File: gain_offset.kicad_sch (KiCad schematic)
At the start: 30 parts, among them U3 AD8337BCPZ-REEL-ND, U4 LMH6551MA, U5 AD8337BCPZ-REEL-ND, U7 LMH6551MA

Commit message: Save work on simplifying the desing
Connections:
- net CH2_COMMON is gone; now on net +1V5: C14.1, U4.2 (VCM)
- net CH1_COMMON renamed +1V5
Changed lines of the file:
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@@
 		)
 	)
-	(global_label "CH2_COMMON"
-		(shape input)
-		(at 168.91 113.03 180)
+	(global_label "AN_TRIGGER_CH1"
+		(shape output)
+		(at 138.43 38.1 0)
 		(fields_autoplaced yes)
 		(effects
@@
 				(size 1.27 1.27)
 			)
-			(justify right)
+			(justify left)
 		)
 		(property "Intersheetrefs" "${INTERSHEET_REFS}"
-			(at 152.9829 113.03 0)
-			(effects
-				(font
-					(size 1.27 1.27)
-				)
-				(justify right)
-				(hide yes)
-			)
-		)
-	)
-	(global_label "AN_TRIGGER_CH1"
-		(shape output)
-		(at 138.43 38.1 0)
+			(at 157.3809 38.1 0)
+			(effects
+				(font
+					(size 1.27 1.27)
+				)
+				(justify left)
+				(hide yes)
+			)
+		)
+	)
+	(global_label "CH2_GAIN_DAC"
+		(shape input)
+		(at 85.09 135.89 180)
 		(fields_autoplaced yes)
 		(effects
@@
 				(size 1.27 1.27)
 			)
-			(justify left)
+			(justify right)
 		)
 		(property "Intersheetrefs" "${INTERSHEET_REFS}"
-			(at 157.3809 38.1 0)
-			(effects
-				(font
-					(size 1.27 1.27)
-				)
-				(justify left)
-				(hide yes)
-			)
-		)
-	)
-	(global_label "CH2_GAIN_DAC"
+			(at 68.4371 135.89 0)
+			(effects
+				(font
+					(size 1.27 1.27)
+				)
+				(justify right)
+				(hide yes)
+			)
+		)
+	)
+	(global_label "CH1_GAIN_DAC"
 		(shape input)
-		(at 85.09 135.89 180)
+		(at 78.74 81.28 180)
 		(fields_autoplaced yes)
 		(effects
@@
 		)
 		(property "Intersheetrefs" "${INTERSHEET_REFS}"
-			(at 68.4371 135.89 0)
+			(at 62.0871 81.28 0)
 			(effects
 				(font
@@
 		)
 	)
-	(global_label "CH1_GAIN_DAC"
+	(global_label "CH1_VGA"
 		(shape input)
-		(at 78.74 81.28 180)
+		(at 41.91 48.26 180)
 		(fields_autoplaced yes)
 		(effects
@@
 		)
 		(property "Intersheetrefs" "${INTERSHEET_REFS}"
-			(at 62.0871 81.28 0)
+			(at 30.7 48.26 0)
 			(effects
 				(font
@@
 		)
 	)
-	(global_label "CH1_VGA"
+	(global_label "CH2_VGA"
 		(shape input)
-		(at 41.91 48.26 180)
+		(at 41.91 100.33 180)
 		(fields_autoplaced yes)
 		(effects
@@
 		)
 		(property "Intersheetrefs" "${INTERSHEET_REFS}"
-			(at 30.7 48.26 0)
+			(at 30.7 100.33 0)
 			(effects
 				(font
@@
 		)
 	)
-	(global_label "CH2_VGA"
-		(shape input)
-		(at 41.91 100.33 180)
+	(global_label "AN_TRIGGER_CH2"
+		(shape output)
+		(at 138.43 90.17 0)
 		(fields_autoplaced yes)
 		(effects
@@
 				(size 1.27 1.27)
 			)
-			(justify right)
+			(justify left)
 		)
 		(property "Intersheetrefs" "${INTERSHEET_REFS}"
-			(at 30.7 100.33 0)
-			(effects
-				(font
-					(size 1.27 1.27)
-				)
-				(justify right)
-				(hide yes)
-			)
-		)
-	)
-	(global_label "AN_TRIGGER_CH2"
+			(at 157.3809 90.17 0)
+			(effects
+				(font
+					(size 1.27 1.27)
+				)
+				(justify left)
+				(hide yes)
+			)
+		)
+	)
+	(global_label "CH2_CH-"
 		(shape output)
-		(at 138.43 90.17 0)
+		(at 254 110.49 0)
 		(fields_autoplaced yes)
 		(effects
@@
 		)
 		(property "Intersheetrefs" "${INTERSHEET_REFS}"
-			(at 157.3809 90.17 0)
+			(at 265.9357 110.49 0)
 			(effects
 				(font
@@
 		)
 	)
-	(global_label "CH1_COMMON"
-		(shape input)
-		(at 168.91 60.96 180)
+	(global_label "CH2_CH+"
+		(shape output)
+		(at 254 120.65 0)
 		(fields_autoplaced yes)
 		(effects
@@
 				(size 1.27 1.27)
 			)
-			(justify right)
-		)
-		(property "Intersheetrefs" "${INTERSHEET_REFS}"
-			(at 152.9829 60.96 0)
-			(effects
-				(font
-					(size 1.27 1.27)
-				)
-				(justify right)
-				(hide yes)
-			)
-		)
-	)
-	(global_label "CH2_CH-"
-		(shape output)
-		(at 254 110.49 0)
-		(fields_autoplaced yes)
-		(effects
-			(font
-				(size 1.27 1.27)
-			)
-			(justify left)
-		)
-		(property "Intersheetrefs" "${INTERSHEET_REFS}"
-			(at 265.9357 110.49 0)
-			(effects
-				(font
-					(size 1.27 1.27)
-				)
-				(justify left)
-				(hide yes)
-			)
-		)
-	)
-	(global_label "CH2_CH+"
-		(shape output)
-		(at 254 120.65 0)
-		(fields_autoplaced yes)
-		(effects
-			(font
-				(size 1.27 1.27)
-			)
 			(justify left)
 		)
@@
 	)
 	(symbol
+		(lib_id "power:+1V5")
+		(at 168.91 113.03 90)
+		(unit 1)
+		(exclude_from_sim no)
+		(in_bom yes)
+		(on_board yes)
+		(dnp no)
+		(fields_autoplaced yes)
+		(property "Reference" "#PWR063"
+			(at 172.72 113.03 0)
+			(effects
+				(font
+					(size 1.27 1.27)
+				)
+				(hide yes)
+			)
+		)
+		(property "Value" "+1V5"
+			(at 165.1 113.0299 90)
+			(effects
+				(font
+					(size 1.27 1.27)
+				)
+				(justify left)
+			)
+		)
+		(property "Footprint" ""
+			(at 168.91 113.03 0)
+			(effects
+				(font
+					(size 1.27 1.27)
+				)
+				(hide yes)
+			)
+		)
+		(property "Datasheet" ""
+			(at 168.91 113.03 0)
+			(effects
+				(font
+					(size 1.27 1.27)
+				)
+				(hide yes)
+			)
+		)
+		(property "Description" "Power symbol creates a global label with name \"+1V5\""
+			(at 168.91 113.03 0)
+			(effects
+				(font
+					(size 1.27 1.27)
+				)
+				(hide yes)
+			)
+		)
+		(pin "1"
+		)
+		(instances
+			(project "DigitalOsciloscope"
+				(path "/553deb7b-4100-40fe-99d2-0c7b4b56aad2/8a4d3ccc-9040-4eb2-98b7-763cffb44d2b"
+					(reference "#PWR063")
+					(unit 1)
+				)
+			)
+		)
+	)
+	(symbol
 		(lib_id "power:GND")
 		(at 105.41 128.27 0)
@@
 					(unit 1)
 				)
+			)
+		)
+	)
+	(symbol
+		(lib_id "power:+1V5")
+		(at 168.91 60.96 90)
+		(unit 1)
+		(exclude_from_sim no)
+		(in_bom yes)
+		(on_board yes)
+		(dnp no)
+		(fields_autoplaced yes)
+		(property "Reference" "#PWR062"
+			(at 172.72 60.96 0)
+			(effects
+				(font
+					(size 1.27 1.27)
+				)
+				(hide yes)
+			)
+		)
+		(property "Value" "+1V5"
+			(at 165.1 60.9599 90)
+			(effects
+				(font
+					(size 1.27 1.27)
+				)
+				(justify left)
+			)
+		)
+		(property "Footprint" ""
+			(at 168.91 60.96 0)
+			(effects
+				(font
+					(size 1.27 1.27)
+				)
+				(hide yes)
+			)
+		)
+		(property "Datasheet" ""
+			(at 168.91 60.96 0)
+			(effects
+				(font
+					(size 1.27 1.27)
+				)
+				(hide yes)
+			)
+		)
+		(property "Description" "Power symbol creates a global label with name \"+1V5\""
+			(at 168.91 60.96 0)
+			(effects
+				(font
+					(size 1.27 1.27)
+				)
+				(hide yes)
+			)
+		)
+		(pin "1"
+		)
+		(instances
+			(project "DigitalOsciloscope"
+				(path "/553deb7b-4100-40fe-99d2-0c7b4b56aad2/8a4d3ccc-9040-4eb2-98b7-763cffb44d2b"
+					(reference "#PWR062")
+					(unit 1)
+				)

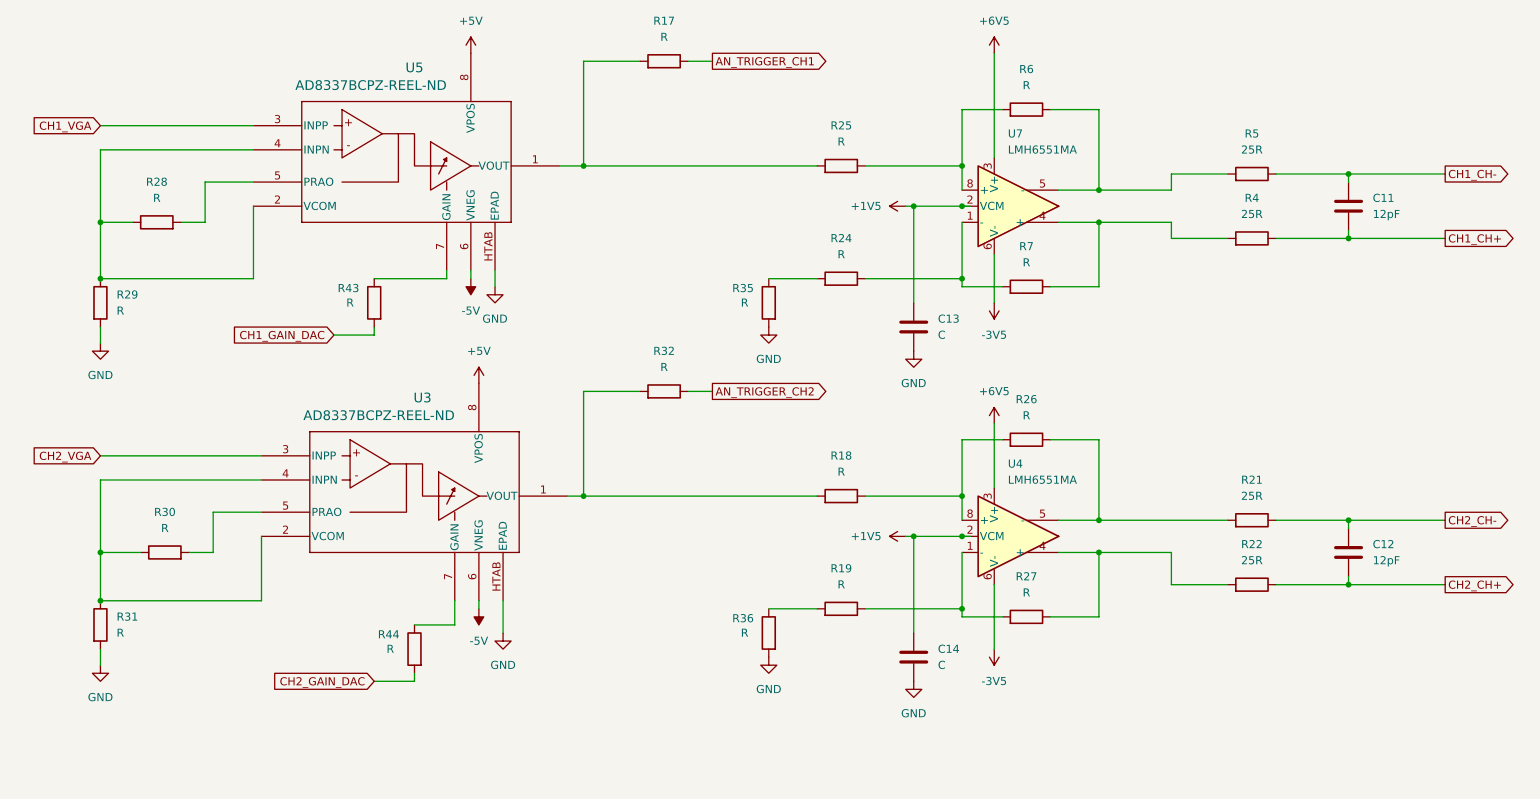
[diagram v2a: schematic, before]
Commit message: Simplifying the design
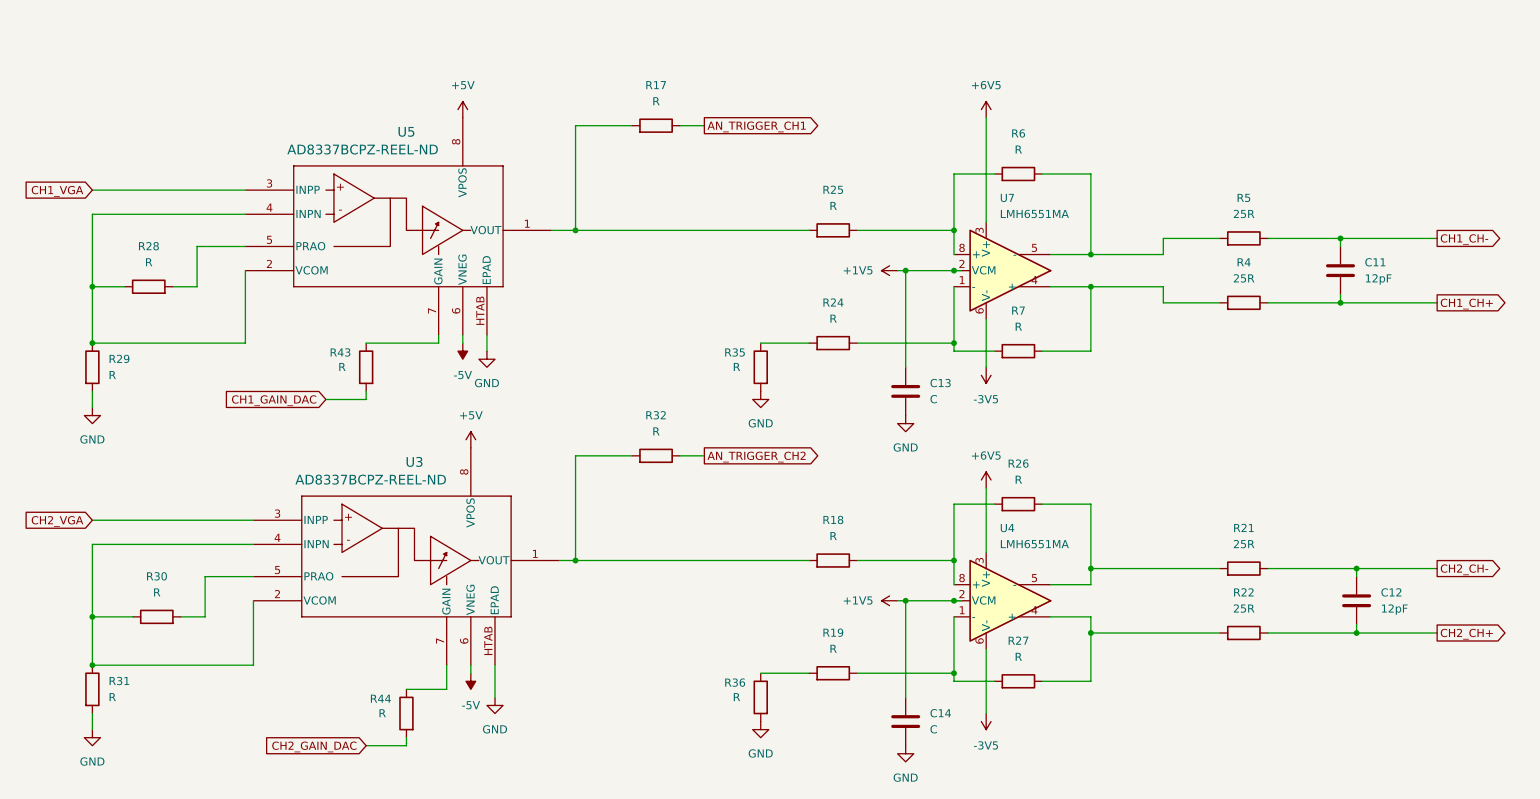
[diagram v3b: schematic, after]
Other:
- moved on the sheet: C11, C12, C13, C14, R17, R18, R19, R21, R22, R24, R25, R26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

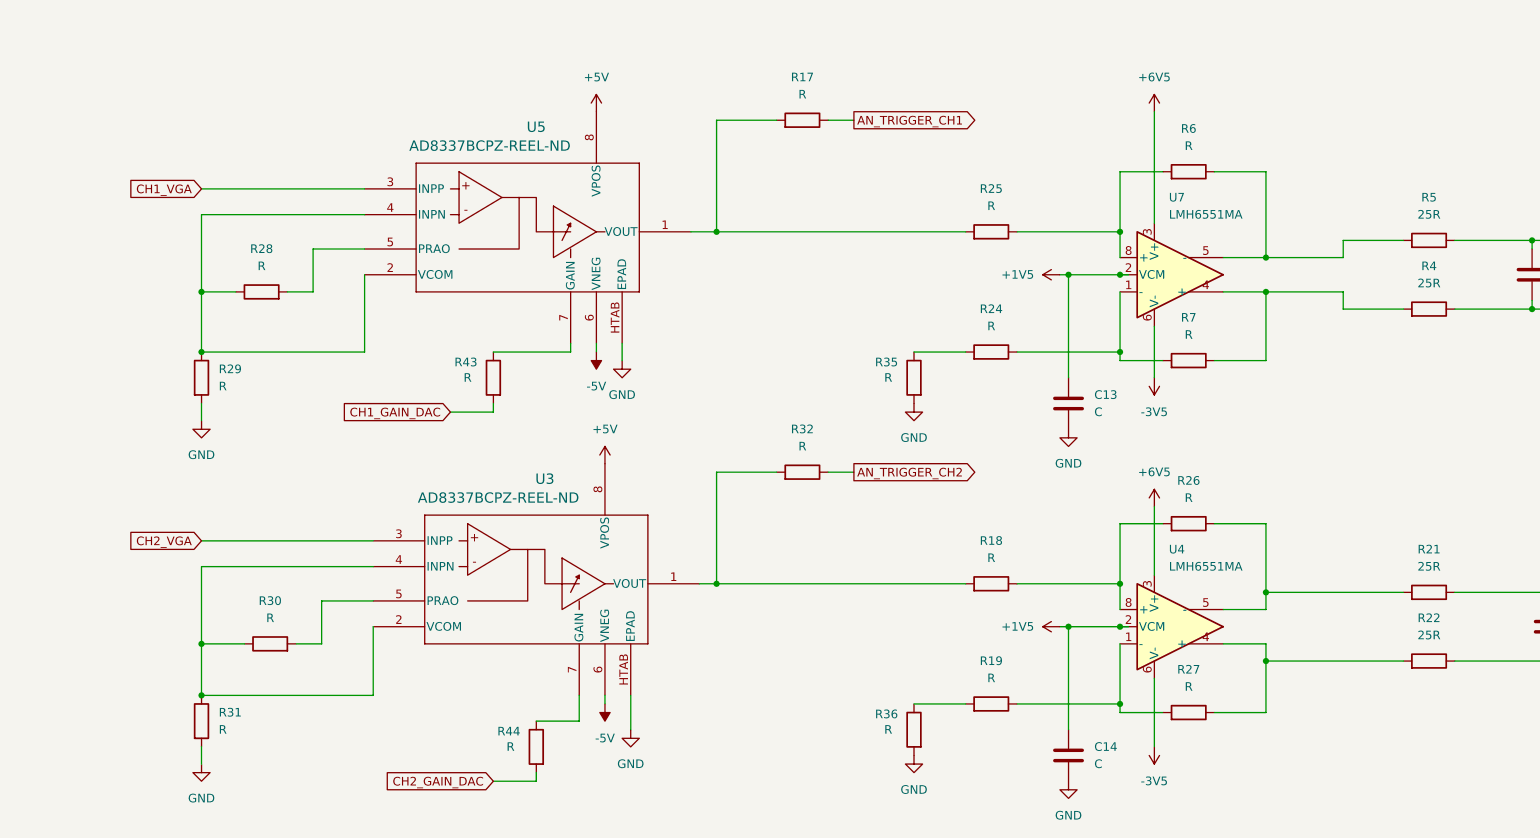
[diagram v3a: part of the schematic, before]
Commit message: Gain on diff amp 0.2
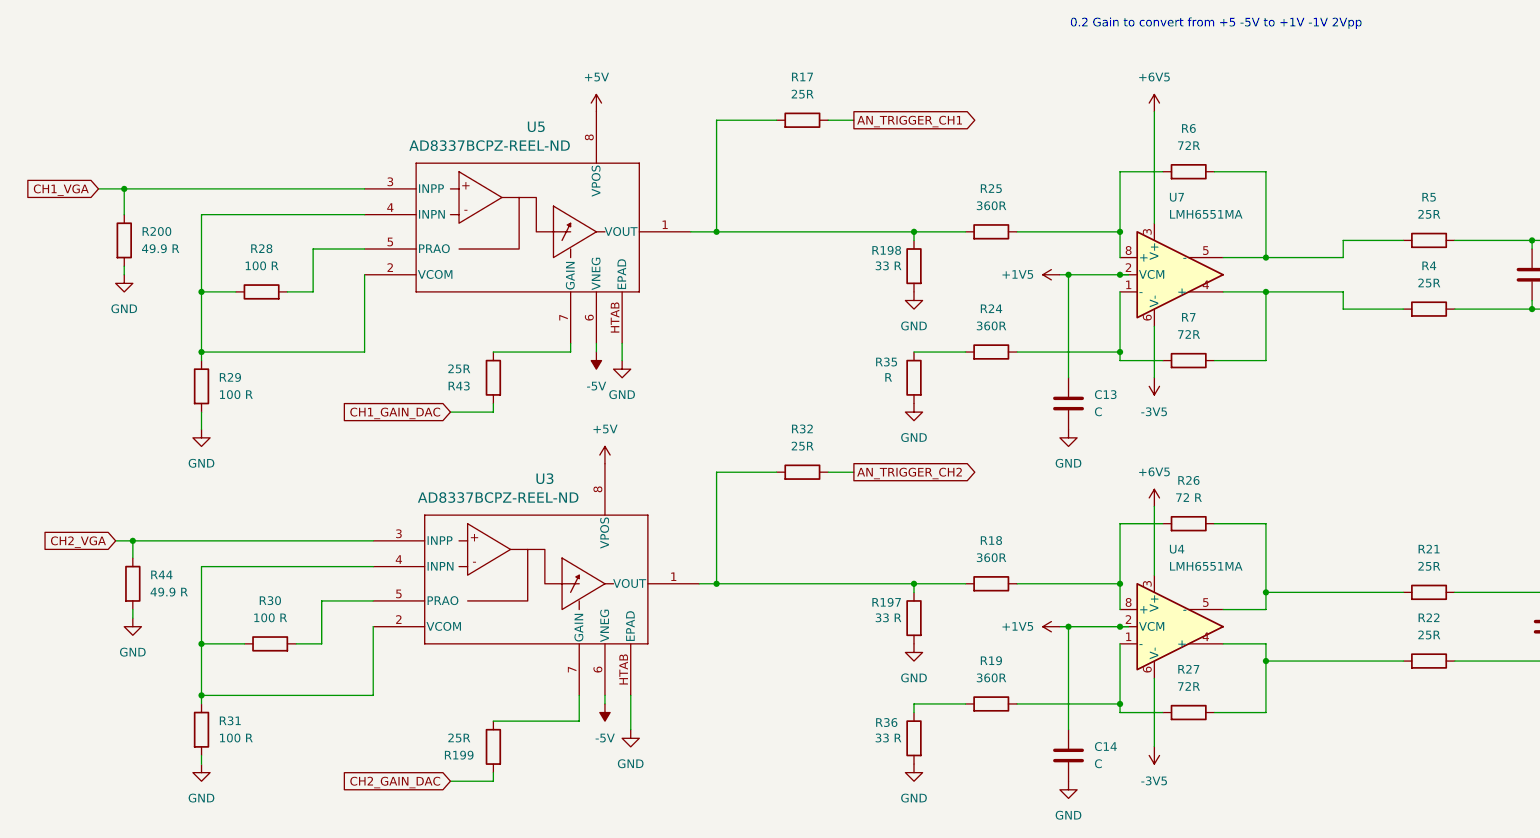
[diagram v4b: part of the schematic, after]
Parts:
- added R197, R198: 33 R, symbol Device:R
- added R199: 25R, Resistor_SMD:R_0402_1005Metric_Pad0.72x0.64mm_HandSolder, symbol Device:R
- added R200: 49.9 R, symbol Device:R
- R17, R32, R43: value R -> 25R; footprint (none) -> Resistor_SMD:R_0402_1005Metric_Pad0.72x0.64mm_HandSolder
- R18, R19, R24, R25: value R -> 360R
- R26: value R -> 72 R
- R27, R6, R7: value R -> 72R
- R28, R29, R30, R31: value R -> 100 R
- R36: value R -> 33 R
- R44: value R -> 49.9 R
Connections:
- net CH1_VGA: now also R200.1
- net CH2_GAIN_DAC: now also R199.2; no longer R44.2
- net CH2_VGA: now also R44.1
- net GND: now also R44.2, R197.2, R198.2, R200.2
- net at R17.2, R25.2, U5.1 (VOUT): now also R198.1
- net at R18.2, R32.2, U3.1 (VOUT): now also R197.1
- net at U3.7 (GAIN): now also R199.1; no longer R44.1
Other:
- note added: "0.2 Gain to convert from +5 -5V to +1V -1V 2Vpp"
- moved on the sheet: R31, R36
